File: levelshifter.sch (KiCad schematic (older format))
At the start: 5 parts, among them U801 HN1C01FU

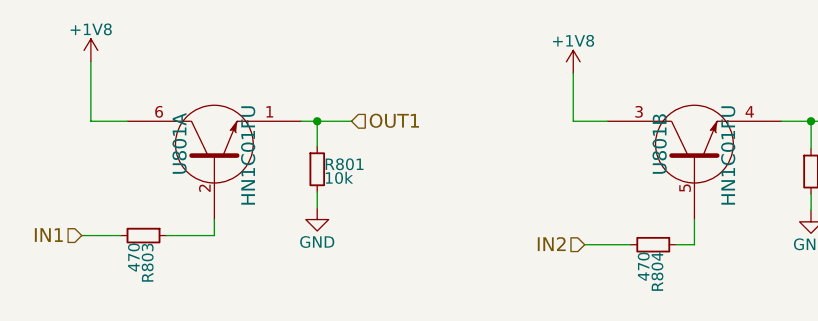
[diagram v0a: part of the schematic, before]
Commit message: Assign a lot of footprints, fix l78l33abu part (input and output were reversed)
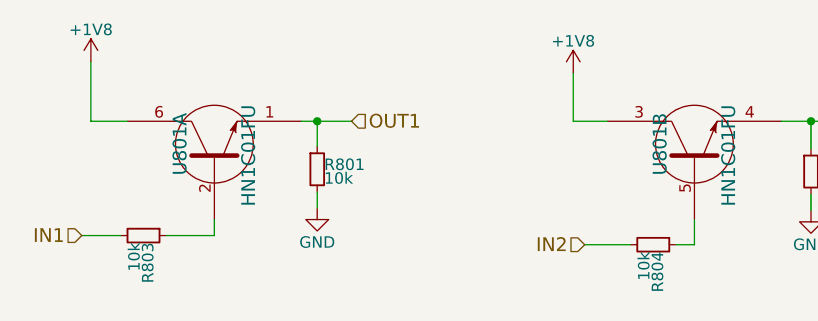
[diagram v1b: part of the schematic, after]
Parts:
- R801, R802: footprint (none) -> Resistors_SMD:R_0603_HandSoldering
- R803, R804: value 470 -> 10k; footprint (none) -> Resistors_SMD:R_0603_HandSoldering
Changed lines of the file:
@@
 $EndComp
 $Comp
-L +1V8 #PWR079
+L +1V8 #PWR080
 U 1 1 5A51803E
 P 4510 2000
-F 0 "#PWR079" H 4510 1850 50  0001 C CNN
+F 0 "#PWR080" H 4510 1850 50  0001 C CNN
 F 1 "+1V8" H 4510 2140 50  0000 C CNN
 F 2 "" H 4510 2000 50  0001 C CNN
@@
 $EndComp
 $Comp
-L +1V8 #PWR080
+L +1V8 #PWR081
 U 1 1 5A5180B2
 P 6620 2050
-F 0 "#PWR080" H 6620 1900 50  0001 C CNN
+F 0 "#PWR081" H 6620 1900 50  0001 C CNN
 F 1 "+1V8" H 6620 2190 50  0000 C CNN
 F 2 "" H 6620 2050 50  0001 C CNN
@@
 F 0 "R801" H 5530 2490 50  0000 L CNN
 F 1 "10k" H 5530 2430 50  0000 L CNN
-F 2 "" H 5500 2470 50  0001 C CNN
+F 2 "Resistors_SMD:R_0603_HandSoldering" H 5500 2470 50  0001 C CNN
 F 3 "" H 5500 2470 50  0001 C CNN
 	1    5500 2470
@@
 P 4740 2760
 F 0 "R803" H 4770 2780 50  0000 L CNN
-F 1 "470" H 4770 2720 50  0000 L CNN
-F 2 "" H 4740 2760 50  0001 C CNN
+F 1 "10k" H 4770 2720 50  0000 L CNN
+F 2 "Resistors_SMD:R_0603_HandSoldering" H 4740 2760 50  0001 C CNN
 F 3 "" H 4740 2760 50  0001 C CNN
 	1    4740 2760
@@
 F 0 "R802" H 7690 2500 50  0000 L CNN
 F 1 "10k" H 7690 2440 50  0000 L CNN
-F 2 "" H 7660 2480 50  0001 C CNN
+F 2 "Resistors_SMD:R_0603_HandSoldering" H 7660 2480 50  0001 C CNN
 F 3 "" H 7660 2480 50  0001 C CNN
 	1    7660 2480
@@
 P 6970 2800
 F 0 "R804" H 7000 2820 50  0000 L CNN
-F 1 "470" H 7000 2760 50  0000 L CNN
-F 2 "" H 6970 2800 50  0001 C CNN
+F 1 "10k" H 7000 2760 50  0000 L CNN
+F 2 "Resistors_SMD:R_0603_HandSoldering" H 6970 2800 50  0001 C CNN
 F 3 "" H 6970 2800 50  0001 C CNN
 	1    6970 2800
@@
 $EndComp
 $Comp
-L GND #PWR081
+L GND #PWR082
 U 1 1 5A5183D2
 P 5500 2640
-F 0 "#PWR081" H 5500 2390 50  0001 C CNN
+F 0 "#PWR082" H 5500 2390 50  0001 C CNN
 F 1 "GND" H 5500 2490 50  0000 C CNN
 F 2 "" H 5500 2640 50  0001 C CNN
@@
 $EndComp
 $Comp
-L GND #PWR082
+L GND #PWR083
 U 1 1 5A5183F6
 P 7660 2650
-F 0 "#PWR082" H 7660 2400 50  0001 C CNN
+F 0 "#PWR083" H 7660 2400 50  0001 C CNN
 F 1 "GND" H 7660 2500 50  0000 C CNN
 F 2 "" H 7660 2650 50  0001 C CNN

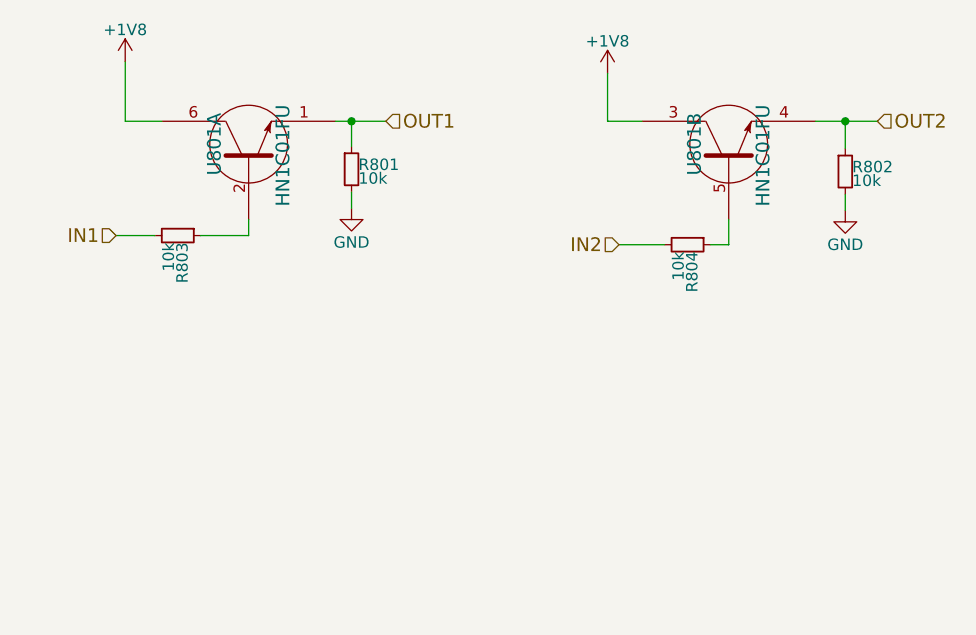
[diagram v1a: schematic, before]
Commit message: Finished circuit layout (for the RF board)
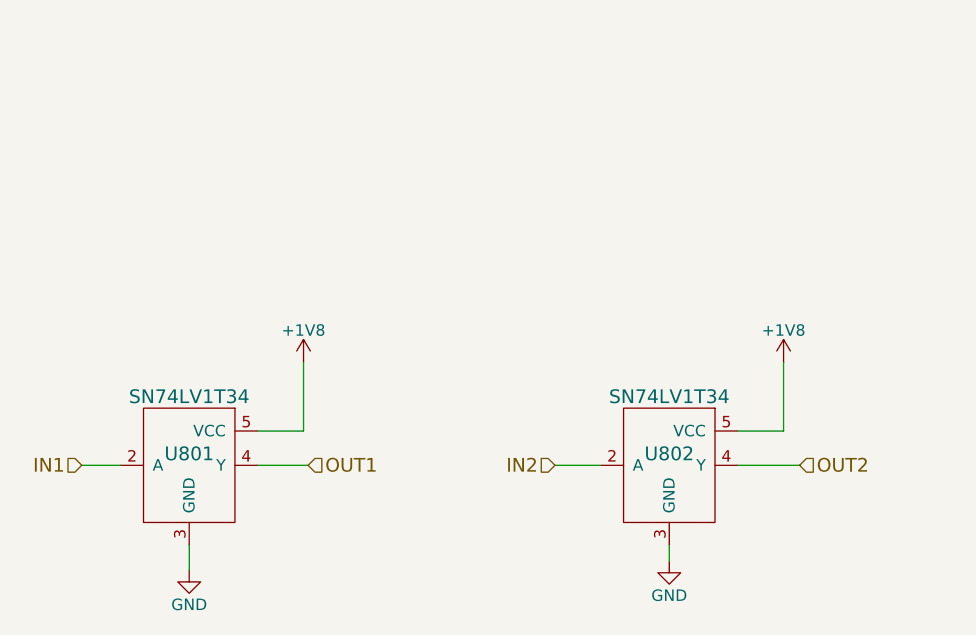
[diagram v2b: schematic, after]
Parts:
- removed R801, R802, R803, R804: 10k, Resistors_SMD:R_0603_HandSoldering, symbol R_Small
- removed U801: HN1C01FU, symbol HN1C01FU
- added U801, U802: SN74LV1T34, TO_SOT_Packages_SMD:SOT-23-5_HandSoldering, symbol SN74LV1T34
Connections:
- net +1V8: now also U801.5 (VCC), U802.5 (VCC)
- net GND: now also U801.3 (GND), U802.3 (GND)
- net IN1: now also U801.2 (A)
- net IN2: now also U802.2 (A)
- net OUT1: now also U801.4 (Y)
- net OUT2: now also U802.4 (Y)
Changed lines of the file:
@@
 LIBS:radar-cache
 LIBS:hn1c01fu
+LIBS:sn74lv1t34
+LIBS:adf4153a
+LIBS:mc2016k30
+LIBS:cp0402q5425entr
 EELAYER 25 0
 EELAYER END
 $Descr A4 11693 8268
 encoding utf-8
-Sheet 8 8
+Sheet 7 8
 Title ""
 Date ""
@@
 $EndDescr
 $Comp
-L HN1C01FU U801
-U 1 1 5A517DB0
-P 5050 2360
-F 0 "U801" H 5050 2510 60  0000 C CNN
-F 1 "HN1C01FU" H 5000 2210 60  0000 C CNN
-F 2 "" H 5050 2360 60  0001 C CNN
-F 3 "" H 5050 2360 60  0001 C CNN
-	1    5050 2360
-	0    -1   -1   0
-$EndComp
-$Comp
-L HN1C01FU U801
-U 2 1 5A517DF9
-P 7150 2360
-F 0 "U801" H 7150 2510 60  0000 C CNN
-F 1 "HN1C01FU" H 7100 2210 60  0000 C CNN
-F 2 "" H 7150 2360 60  0001 C CNN
-F 3 "" H 7150 2360 60  0001 C CNN
-	2    7150 2360
-	0    -1   -1   0
-$EndComp
-$Comp
 L +1V8 #PWR080
 U 1 1 5A51803E
-P 4510 2000
-F 0 "#PWR080" H 4510 1850 50  0001 C CNN
-F 1 "+1V8" H 4510 2140 50  0000 C CNN
-F 2 "" H 4510 2000 50  0001 C CNN
-F 3 "" H 4510 2000 50  0001 C CNN
-	1    4510 2000
+P 5290 3315
+F 0 "#PWR080" H 5290 3165 50  0001 C CNN
+F 1 "+1V8" H 5290 3455 50  0000 C CNN
+F 2 "" H 5290 3315 50  0001 C CNN
+F 3 "" H 5290 3315 50  0001 C CNN
+	1    5290 3315
+	1    0    0    -1
+$EndComp
+Wire Wire Line
+	5290 3315 5290 3615
+$Comp
+L GND #PWR081
+U 1 1 5A5183D2
+P 4790 4225
+F 0 "#PWR081" H 4790 3975 50  0001 C CNN
+F 1 "GND" H 4790 4075 50  0000 C CNN
+F 2 "" H 4790 4225 50  0001 C CNN
+F 3 "" H 4790 4225 50  0001 C CNN
+	1    4790 4225
 	1    0    0    -1
 $EndComp
 $Comp
-L +1V8 #PWR081
-U 1 1 5A5180B2
-P 6620 2050
-F 0 "#PWR081" H 6620 1900 50  0001 C CNN
-F 1 "+1V8" H 6620 2190 50  0000 C CNN
-F 2 "" H 6620 2050 50  0001 C CNN
-F 3 "" H 6620 2050 50  0001 C CNN
-	1    6620 2050
+L GND #PWR082
+U 1 1 5A5183F6
+P 6890 4185
+F 0 "#PWR082" H 6890 3935 50  0001 C CNN
+F 1 "GND" H 6890 4035 50  0000 C CNN
+F 2 "" H 6890 4185 50  0001 C CNN
+F 3 "" H 6890 4185 50  0001 C CNN
+	1    6890 4185
 	1    0    0    -1
 $EndComp
 Wire Wire Line
-	4510 2000 4510 2260
+	4320 3765 4490 3765
 Wire Wire Line
-	4510 2260 4670 2260
+	5090 3765 5310 3765
 Wire Wire Line
-	6620 2050 6620 2260
+	6390 3765 6590 3765
 Wire Wire Line
-	6620 2260 6770 2260
+	7190 3765 7460 3765
+Wire Wire Line
+	6890 4185 6890 4115
+Text HLabel 4320 3765 0    60   Input ~ 0
+IN1
+Text HLabel 5310 3765 2    60   Input ~ 0
+OUT1
+Text HLabel 6390 3765 0    60   Input ~ 0
+IN2
+Text HLabel 7460 3765 2    60   Input ~ 0
+OUT2
+Wire Wire Line
+	4790 4115 4790 4225
+Wire Wire Line
+	5290 3615 5090 3615
 $Comp
-L R_Small R801
-U 1 1 5A5180D7
-P 5500 2470
-F 0 "R801" H 5530 2490 50  0000 L CNN
-F 1 "10k" H 5530 2430 50  0000 L CNN
-F 2 "Resistors_SMD:R_0603_HandSoldering" H 5500 2470 50  0001 C CNN
-F 3 "" H 5500 2470 50  0001 C CNN
-	1    5500 2470
+L +1V8 #PWR083
+U 1 1 5A7E814C
+P 7390 3315
+F 0 "#PWR083" H 7390 3165 50  0001 C CNN
+F 1 "+1V8" H 7390 3455 50  0000 C CNN
+F 2 "" H 7390 3315 50  0001 C CNN
+F 3 "" H 7390 3315 50  0001 C CNN
+	1    7390 3315
+	1    0    0    -1
+$EndComp
+Wire Wire Line
+	7390 3315 7390 3615
+Wire Wire Line
+	7390 3615 7190 3615
+$Comp
+L SN74LV1T34 U801
+U 1 1 5A7E7EF8
+P 4790 3715
+F 0 "U801" H 4790 3715 60  0000 C CNN
+F 1 "SN74LV1T34" H 4790 3965 60  0000 C CNN
+F 2 "TO_SOT_Packages_SMD:SOT-23-5_HandSoldering" H 4790 3715 60  0001 C CNN
+F 3 "http://www.ti.com/lit/ds/symlink/sn74lv1t34.pdf" H 4790 3715 60  0001 C CNN
+	1    4790 3715
 	1    0    0    -1
 $EndComp
 $Comp
-L R_Small R803
-U 1 1 5A518161
-P 4740 2760
-F 0 "R803" H 4770 2780 50  0000 L CNN
-F 1 "10k" H 4770 2720 50  0000 L CNN
-F 2 "Resistors_SMD:R_0603_HandSoldering" H 4740 2760 50  0001 C CNN
-F 3 "" H 4740 2760 50  0001 C CNN
-	1    4740 2760
-	0    1    1    0
-$EndComp
-$Comp
-L R_Small R802
-U 1 1 5A51825F
-P 7660 2480
-F 0 "R802" H 7690 2500 50  0000 L CNN
-F 1 "10k" H 7690 2440 50  0000 L CNN
-F 2 "Resistors_SMD:R_0603_HandSoldering" H 7660 2480 50  0001 C CNN
-F 3 "" H 7660 2480 50  0001 C CNN
-	1    7660 2480
+L SN74LV1T34 U802
+U 1 1 5A7E7FA3
+P 6890 3715
+F 0 "U802" H 6890 3715 60  0000 C CNN
+F 1 "SN74LV1T34" H 6890 3965 60  0000 C CNN
+F 2 "TO_SOT_Packages_SMD:SOT-23-5_HandSoldering" H 6890 3715 60  0001 C CNN
+F 3 "http://www.ti.com/lit/ds/symlink/sn74lv1t34.pdf" H 6890 3715 60  0001 C CNN
+	1    6890 3715
 	1    0    0    -1
 $EndComp
-$Comp
-L R_Small R804
-U 1 1 5A5182DC
-P 6970 2800
-F 0 "R804" H 7000 2820 50  0000 L CNN
-F 1 "10k" H 7000 2760 50  0000 L CNN
-F 2 "Resistors_SMD:R_0603_HandSoldering" H 6970 2800 50  0001 C CNN
-F 3 "" H 6970 2800 50  0001 C CNN
-	1    6970 2800
-	0    1    1    0
-$EndComp
-$Comp
-L GND #PWR082
-U 1 1 5A5183D2
-P 5500 2640
-F 0 "#PWR082" H 5500 2390 50  0001 C CNN
-F 1 "GND" H 5500 2490 50  0000 C CNN
-F 2 "" H 5500 2640 50  0001 C CNN
-F 3 "" H 5500 2640 50  0001 C CNN
-	1    5500 2640
-	1    0    0    -1
-$EndComp
-$Comp
-L GND #PWR083
-U 1 1 5A5183F6
-P 7660 2650
-F 0 "#PWR083" H 7660 2400 50  0001 C CNN
-F 1 "GND" H 7660 2500 50  0000 C CNN
-F 2 "" H 7660 2650 50  0001 C CNN
-F 3 "" H 7660 2650 50  0001 C CNN
-	1    7660 2650
-	1    0    0    -1
-$EndComp
-Wire Wire Line
-	4470 2760 4640 2760
-Wire Wire Line
-	4840 2760 5050 2760
-Wire Wire Line
-	5050 2760 5050 2690
-Wire Wire Line
-	5500 2570 5500 2640
-Wire Wire Line
-	5500 2370 5500 2260
-Wire Wire Line
-	5430 2260 5650 2260
-Connection ~ 5500 2260
-Wire Wire Line
-	6670 2800 6870 2800
-Wire Wire Line
-	7070 2800 7150 2800
-Wire Wire Line
-	7150 2800 7150 2690
-Wire Wire Line
-	7530 2260 7800 2260
-Wire Wire Line
-	7660 2260 7660 2380
-Wire Wire Line
-	7660 2650 7660 2580
-Connection ~ 7660 2260
-Text HLabel 4470 2760 0    60   Input ~ 0
-IN1
-Text HLabel 5650 2260 2    60   Input ~ 0
-OUT1
-Text HLabel 6670 2800 0    60   Input ~ 0
-IN2
-Text HLabel 7800 2260 2    60   Input ~ 0
-OUT2
 $EndSCHEMATC
